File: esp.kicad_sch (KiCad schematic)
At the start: 119 parts, among them J1 Barrel_Jack, J11 Barrel_Jack, J12 Barrel_Jack, J13 Barrel_Jack, J14 Barrel_Jack, J2 8P8C_Shielded, J21 8P8C_Shielded, J27 Barrel_Jack, J3 Barrel_Jack, J38 8P8C_Shielded, J39 Barrel_Jack, J4 Barrel_Jack, J40 Barrel_Jack, J42 Barrel_Jack, J5 Barrel_Jack, J7 Barrel_Jack_MountingPin, K1 RT314A24, K5 RT314A24, K6 SRD-05VDC-SL-C, P1 Conn_WallPlug_Earth, Q3 MOSFET-NCHANNELSMD, Q4 MOSFET-NCHANNELSMD, Q5 MOSFET-NCHANNELSMD, Q6 NPN, SW1 SW_SPDT_MSM, U1 ESP32-S2-WROVER, U14 L298N, U15 PCF8574ATS, U16 L298N, U17 L298N, U18 NID30S48-24, U19 PCA9685PW, U2 TCA9548ARGER, U20 PCF8574ATS, U21 PC357_OPTO, U3 TCA9548ARGER, U4 BME280, U5 PCF8574ATS, U6 L298N, U7 OKI-78SR-12_1.0-W36H-C, U8 OKI-78SR-5_1.5-W36-C, U9 OKI-78SR-3.3_1.5-W36H-C

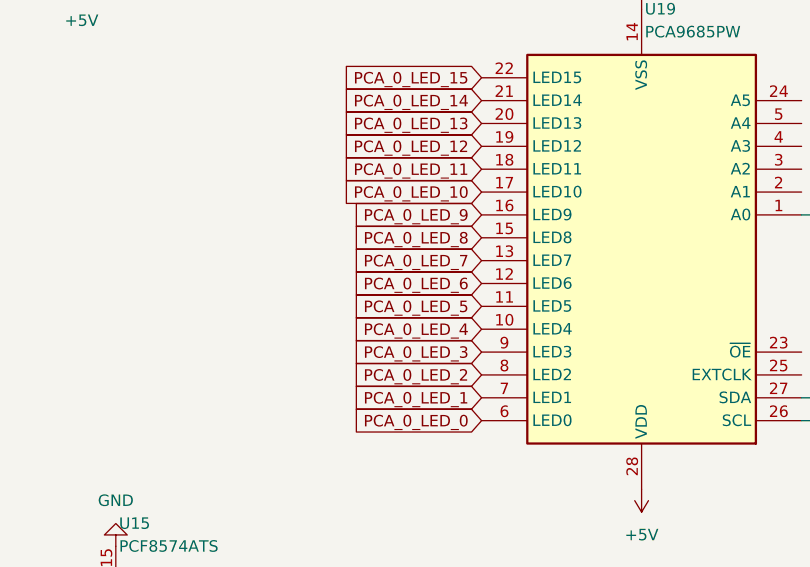
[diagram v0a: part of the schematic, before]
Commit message: PCB can be built, naming issues
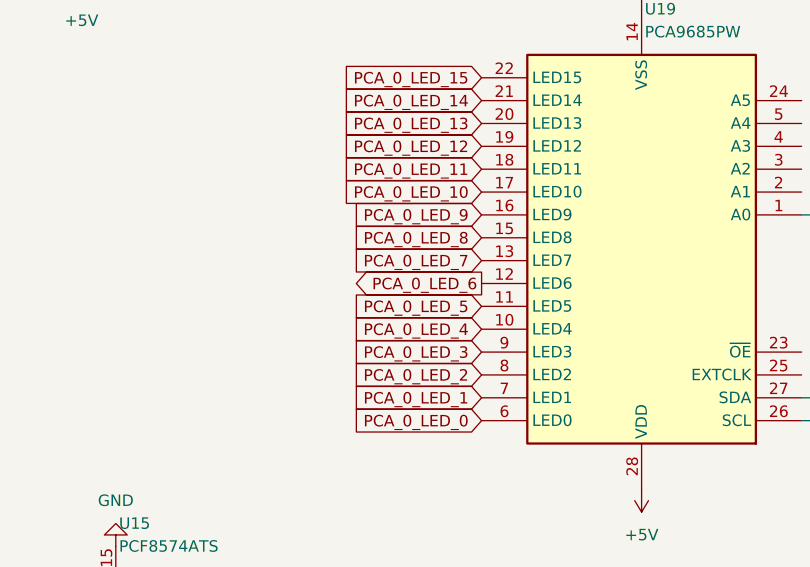
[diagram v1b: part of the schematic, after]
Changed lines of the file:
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@@
     )
   )
-  (global_label "PCA_0_LED_6" (shape input) (at 435.61 405.13 180) (fields_autoplaced)
+  (global_label "PCA_0_LED_6" (shape output) (at 435.61 405.13 180) (fields_autoplaced)
     (effects (font (size 1.27 1.27)) (justify right))
     (property "Intersheetrefs" "${INTERSHEET_REFS}" (at 420.2273 405.13 0)

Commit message: slimmed down and spread out pcb
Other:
- moved on the sheet: J38, K1
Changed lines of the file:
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@@
     (stroke (width 0) (type default))
   )
-  (wire (pts (xy 438.15 231.14) (xy 454.66 231.14))
+  (wire (pts (xy 435.61 229.87) (xy 454.66 229.87))
     (stroke (width 0) (type default))
   )
@@
     (stroke (width 0) (type default))
   )
+  (wire (pts (xy 454.66 229.87) (xy 454.66 231.14))
+    (stroke (width 0) (type default))
+  )
   (wire (pts (xy 284.48 351.79) (xy 270.51 351.79))
     (stroke (width 0) (type default))
@@
     )
   )
-  (global_label "TCA_2_SD7" (shape input) (at 454.66 231.14 0) (fields_autoplaced)
+  (global_label "TCA_2_SD7" (shape input) (at 454.66 229.87 0) (fields_autoplaced)
     (effects (font (size 1.27 1.27)) (justify left))
-    (property "Intersheetrefs" "${INTERSHEET_REFS}" (at 467.8051 231.14 0)
+    (property "Intersheetrefs" "${INTERSHEET_REFS}" (at 467.8051 229.87 0)
       (effects (font (size 1.27 1.27)) (justify left) hide)
     )
@@
     )
   )
-  (symbol (lib_id "Relay:RT314A24") (at 430.53 204.47 0) (unit 1)
+  (symbol (lib_id "Relay:RT314A24") (at 426.72 204.47 0) (unit 1)
     (in_bom yes) (on_board yes) (dnp no) (fields_autoplaced)
-    (property "Reference" "K1" (at 441.96 203.2 0)
+    (property "Reference" "K1" (at 438.15 203.2 0)
       (effects (font (size 1.27 1.27)) (justify left))
     )
-    (property "Value" "RT314A24" (at 441.96 205.74 0)
+    (property "Value" "RT314A24" (at 438.15 205.74 0)
       (effects (font (size 1.27 1.27)) (justify left))
     )
-    (property "Footprint" "Relay_THT:Relay_1P1T_NO_10x24x18.8mm_Panasonic_ADW11xxxxW_THT" (at 469.9 205.74 0)
+    (property "Footprint" "Relay_THT:Relay_1P1T_NO_10x24x18.8mm_Panasonic_ADW11xxxxW_THT" (at 466.09 205.74 0)
       (effects (font (size 1.27 1.27)) hide)
     )
-    (property "Datasheet" "https://www.te.com/commerce/DocumentDelivery/DDEController?Action=srchrtrv&DocNm=RT1_bistable&DocType=DS&DocLang=English" (at 430.53 204.47 0)
+    (property "Datasheet" "https://www.te.com/commerce/DocumentDelivery/DDEController?Action=srchrtrv&DocNm=RT1_bistable&DocType=DS&DocLang=English" (at 426.72 204.47 0)
       (effects (font (size 1.27 1.27)) hide)
     )
@@
     )
   )
-  (symbol (lib_id "Connector:8P8C_Shielded") (at 427.99 241.3 0) (unit 1)
+  (symbol (lib_id "Connector:8P8C_Shielded") (at 425.45 240.03 0) (unit 1)
     (in_bom yes) (on_board yes) (dnp no) (fields_autoplaced)
-    (property "Reference" "J38" (at 427.99 223.52 0)
+    (property "Reference" "J38" (at 425.45 222.25 0)
       (effects (font (size 1.27 1.27)))
     )
-    (property "Value" "8P8C_Shielded" (at 427.99 226.06 0)
+    (property "Value" "8P8C_Shielded" (at 425.45 224.79 0)
       (effects (font (size 1.27 1.27)))
     )
-    (property "Footprint" "Connector_RJ:RJ45_HALO_HFJ11-x2450HRL_Horizontal" (at 427.99 240.665 90)
+    (property "Footprint" "Connector_RJ:RJ45_HALO_HFJ11-x2450HRL_Horizontal" (at 425.45 239.395 90)
       (effects (font (size 1.27 1.27)) hide)
     )
-    (property "Datasheet" "~" (at 427.99 240.665 90)
+    (property "Datasheet" "~" (at 425.45 239.395 90)
       (effects (font (size 1.27 1.27)) hide)
     )
@@
     )
   )
-  (sheet (at -44.45 247.65) (size 118.11 41.91) (fields_autoplaced)
+  (sheet (at 29.21 278.13) (size 118.11 41.91) (fields_autoplaced)
     (stroke (width 0.1524) (type solid))
     (fill (color 0 0 0 0.0000))
-    (property "Sheetname" "Barrel_Jack" (at -44.45 246.9384 0)
+    (property "Sheetname" "Barrel_Jack" (at 29.21 277.4184 0)
       (effects (font (size 1.27 1.27)) (justify left bottom))
     )
-    (property "Sheetfile" "Barrel_Jack.kicad_sch" (at -44.45 290.1446 0)
+    (property "Sheetfile" "Barrel_Jack.kicad_sch" (at 29.21 320.6246 0)
       (effects (font (size 1.27 1.27)) (justify left top))
     )

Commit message: working scematic with seperated layout
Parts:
- added M1: Motor_DC, symbol Motor:Motor_DC
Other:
- moved on the sheet: BT1, BT2, C2, C3, C4, C5, C6, D10, D11, D12, D13, D14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
